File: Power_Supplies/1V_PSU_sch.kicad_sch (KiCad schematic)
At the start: 8 parts, among them U2 TPS62822DLC

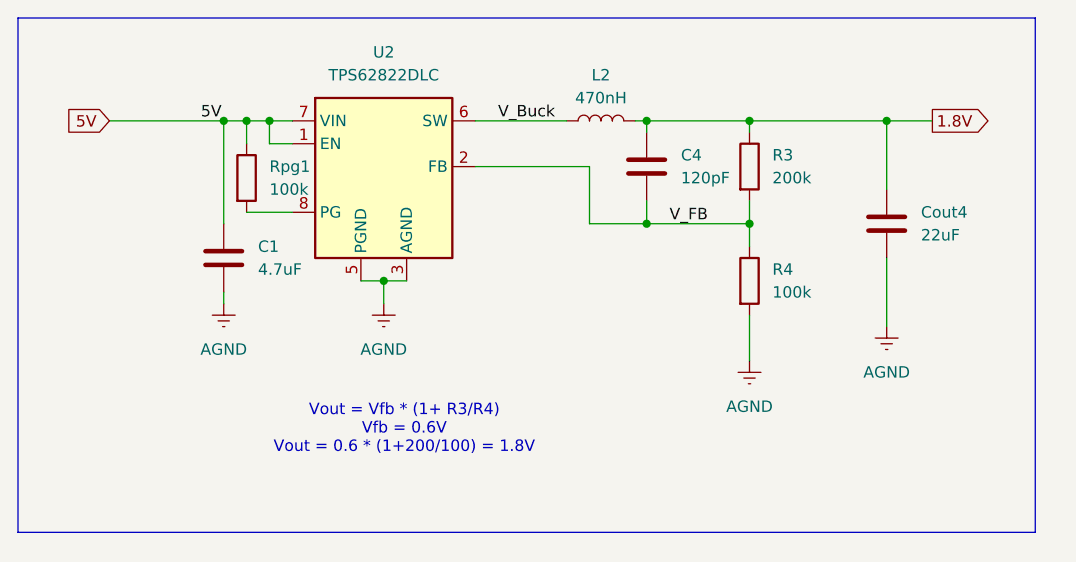
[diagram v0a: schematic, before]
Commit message: Updated power supplies and added DAC circuitry
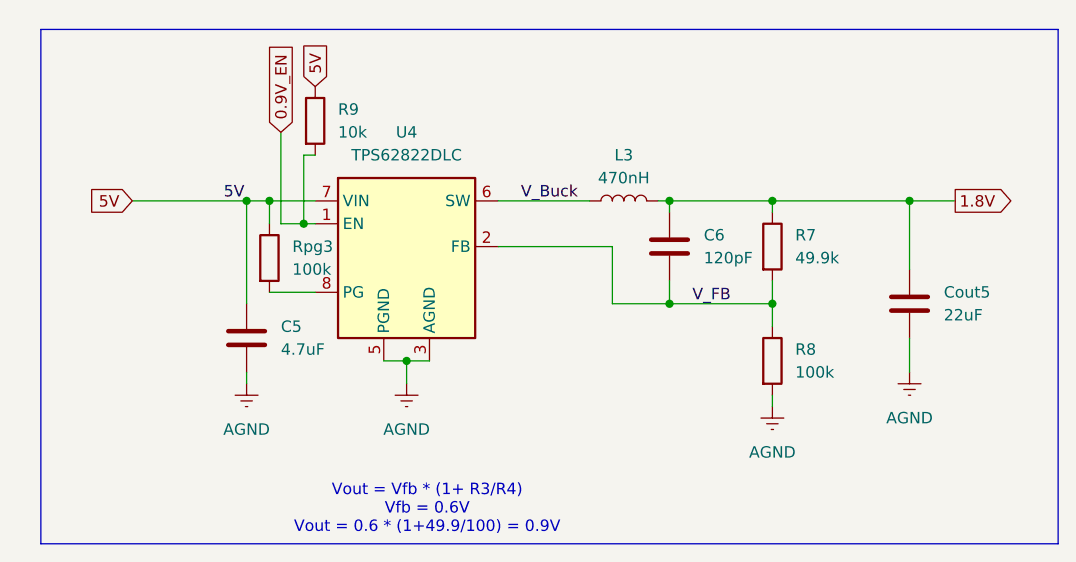
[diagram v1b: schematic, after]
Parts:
- removed C1: 4.7uF, Capacitor_SMD:C_0805_2012Metric, symbol Device:C
- removed C4: 120pF, Capacitor_SMD:C_0402_1005Metric, symbol Device:C
- removed Cout4: 22uF, Capacitor_SMD:C_0805_2012Metric, symbol Device:C
- removed L2: 470nH, Inductor_SMD:L_0805_2012Metric, symbol Device:L
- removed R3: 200k, Resistor_SMD:R_0805_2012Metric, symbol Device:R
- removed R4, Rpg1: 100k, Resistor_SMD:R_0805_2012Metric, symbol Device:R
- removed U2: TPS62822DLC, Package_SON:Texas_VSON-HR-8_1.5x2mm_P0.5mm, symbol Regulator_Switching:TPS62822DLC
- added C5: 4.7uF, Capacitor_SMD:C_0805_2012Metric, symbol Device:C
- added C6: 120pF, Capacitor_SMD:C_0402_1005Metric, symbol Device:C
- added Cout5: 22uF, Capacitor_SMD:C_0805_2012Metric, symbol Device:C
- added L3: 470nH, Inductor_SMD:L_0805_2012Metric, symbol Device:L
- added R7: 49.9k, Resistor_SMD:R_0805_2012Metric, symbol Device:R
- added R8, Rpg3: 100k, Resistor_SMD:R_0805_2012Metric, symbol Device:R
- added R9: 10k, Resistor_SMD:R_0805_2012Metric, symbol Device:R
- added U4: TPS62822DLC, Package_SON:Texas_VSON-HR-8_1.5x2mm_P0.5mm, symbol Regulator_Switching:TPS62822DLC
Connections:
- net 1.8V: now also C6.1, Cout5.1, L3.2, R7.1
- net 5V: now also C5.1, R9.1, Rpg3.1, U4.7 (VIN)
- net AGND: now also C5.2, Cout5.2, R8.2, U4.3 (AGND), U4.5 (PGND)
- net V_Buck: now also L3.1, U4.6 (SW)
- net V_FB: now also C6.2, R7.2, R8.1, U4.2 (FB)
- new net: Rpg3.2, U4.8 (PG)
- new net 0.9V_EN: R9.2, U4.1 (EN)
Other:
- note added: "Vout = Vfb * (1+ R3/R4) Vfb = 0.6V Vout = 0.6 * (1+49.9/100) = 0.9V"
- note removed: "Vout = Vfb * (1+ R3/R4) Vfb = 0.6V Vout = 0.6 * (1+200/100) = 1.8V"

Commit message: Add files via upload
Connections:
- net 1.8V renamed 0.9V
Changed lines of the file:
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@@
 		)
 	)
-	(global_label "1.8V"
+	(global_label "0.9V"
 		(shape output)
 		(at 194.31 63.5 0)

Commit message: big things are coming...
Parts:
- renumbered C6 to C10, C5 to C9, Cout5 to Cout6, R9 to R12, R7 to R13, R8 to R14, Rpg3 to Rpg4, U4 to U7
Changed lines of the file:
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@@
 		(dnp no)
 		(fields_autoplaced yes)
-		(property "Reference" "#PWR09"
+		(property "Reference" "#PWR021"
 			(at 115.57 90.17 0)
 			(effects
@@
 			(project "Power_Supplies"
 				(path "/5266cf9e-da90-4c53-80fd-cf3dbed42632/03d1dd7c-322d-4278-ab1a-c5f616c27c1a"
-					(reference "#PWR09")
+					(reference "#PWR021")
 					(unit 1)
 				)
@@
 		(dnp no)
 		(fields_autoplaced yes)
-		(property "Reference" "#PWR012"
+		(property "Reference" "#PWR024"
 			(at 189.23 88.9 0)
 			(effects
@@
 			(project "Power_Supplies"
 				(path "/5266cf9e-da90-4c53-80fd-cf3dbed42632/03d1dd7c-322d-4278-ab1a-c5f616c27c1a"
-					(reference "#PWR012")
+					(reference "#PWR024")
 					(unit 1)
 				)
@@
 		(dnp no)
 		(fields_autoplaced yes)
-		(property "Reference" "Cout5"
+		(property "Reference" "Cout6"
 			(at 193.04 73.6599 0)
 			(effects
@@
 			(project "Power_Supplies"
 				(path "/5266cf9e-da90-4c53-80fd-cf3dbed42632/03d1dd7c-322d-4278-ab1a-c5f616c27c1a"
-					(reference "Cout5")
+					(reference "Cout6")
 					(unit 1)
 				)
@@
 		(dnp no)
 		(fields_autoplaced yes)
-		(property "Reference" "R9"
+		(property "Reference" "R12"
 			(at 125.73 53.3399 0)
 			(effects
@@
 			(project "Power_Supplies"
 				(path "/5266cf9e-da90-4c53-80fd-cf3dbed42632/03d1dd7c-322d-4278-ab1a-c5f616c27c1a"
-					(reference "R9")
+					(reference "R12")
 					(unit 1)
 				)
@@
 		(dnp no)
 		(fields_autoplaced yes)
-		(property "Reference" "#PWR010"
+		(property "Reference" "#PWR022"
 			(at 133.35 90.17 0)
 			(effects
@@
 			(project "Power_Supplies"
 				(path "/5266cf9e-da90-4c53-80fd-cf3dbed42632/03d1dd7c-322d-4278-ab1a-c5f616c27c1a"
-					(reference "#PWR010")
+					(reference "#PWR022")
 					(unit 1)
 				)
@@
 		(dnp no)
 		(fields_autoplaced yes)
-		(property "Reference" "U4"
+		(property "Reference" "U7"
 			(at 133.35 55.88 0)
 			(effects
@@
 			(project "Power_Supplies"
 				(path "/5266cf9e-da90-4c53-80fd-cf3dbed42632/03d1dd7c-322d-4278-ab1a-c5f616c27c1a"
-					(reference "U4")
+					(reference "U7")
 					(unit 1)
 				)
@@
 		(dnp no)
 		(fields_autoplaced yes)
-		(property "Reference" "R8"
+		(property "Reference" "R14"
 			(at 176.53 80.0099 0)
 			(effects
@@
 			(project "Power_Supplies"
 				(path "/5266cf9e-da90-4c53-80fd-cf3dbed42632/03d1dd7c-322d-4278-ab1a-c5f616c27c1a"
-					(reference "R8")
+					(reference "R14")
 					(unit 1)
 				)
@@
 		(dnp no)
 		(fields_autoplaced yes)
-		(property "Reference" "C6"
+		(property "Reference" "C10"
 			(at 166.37 67.3099 0)
 			(effects
@@
 			(project "Power_Supplies"
 				(path "/5266cf9e-da90-4c53-80fd-cf3dbed42632/03d1dd7c-322d-4278-ab1a-c5f616c27c1a"
-					(reference "C6")
+					(reference "C10")
 					(unit 1)
 				)
@@
 		(dnp no)
 		(fields_autoplaced yes)
-		(property "Reference" "R7"
+		(property "Reference" "R13"
 			(at 176.53 67.3099 0)
 			(effects
@@
 			(project "Power_Supplies"
 				(path "/5266cf9e-da90-4c53-80fd-cf3dbed42632/03d1dd7c-322d-4278-ab1a-c5f616c27c1a"
-					(reference "R7")
+					(reference "R13")
 					(unit 1)
 				)
@@
 		(dnp no)
 		(fields_autoplaced yes)
-		(property "Reference" "#PWR011"
+		(property "Reference" "#PWR023"
 			(at 173.99 92.71 0)
 			(effects
@@
 			(project "Power_Supplies"
 				(path "/5266cf9e-da90-4c53-80fd-cf3dbed42632/03d1dd7c-322d-4278-ab1a-c5f616c27c1a"
-					(reference "#PWR011")
+					(reference "#PWR023")
 					(unit 1)
 				)
@@
 		(dnp no)
 		(fields_autoplaced yes)
-		(property "Reference" "C5"
+		(property "Reference" "C9"
 			(at 119.38 77.4699 0)
 			(effects
@@
 			(project "Power_Supplies"
 				(path "/5266cf9e-da90-4c53-80fd-cf3dbed42632/03d1dd7c-322d-4278-ab1a-c5f616c27c1a"
-					(reference "C5")
+					(reference "C9")
 					(unit 1)
 				)
@@
 		(dnp no)
 		(fields_autoplaced yes)
-		(property "Reference" "Rpg3"
+		(property "Reference" "Rpg4"
 			(at 120.65 68.5799 0)
 			(effects
@@
 			(project "Power_Supplies"
 				(path "/5266cf9e-da90-4c53-80fd-cf3dbed42632/03d1dd7c-322d-4278-ab1a-c5f616c27c1a"
-					(reference "Rpg3")
-					(unit 1)
-				)
+					(reference "Rpg4")
+					(unit 1)
+				)
